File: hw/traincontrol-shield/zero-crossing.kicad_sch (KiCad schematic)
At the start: 3 parts, among them U2 H11AA1

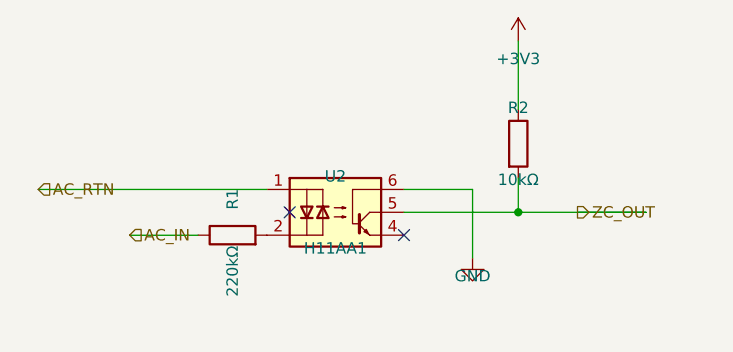
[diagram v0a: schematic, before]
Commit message: Fix U2 (H11AA1) zero-crossing wiring: emitter→GND, base→NC
KiCad symbol coords use y-up convention, so schematic positions
are cy ∓ symbol_y.  Pin 4 (Emitter) is at cy+2.54 (lower-right)
and Pin 6 (Base) is at cy-2.54 (upper-right) — the previous code
had these swapped, connecting GND to the base and NC to the emitter.

Co-Authored-By: Claude Sonnet 4.6 <noreply@anthropic.com>
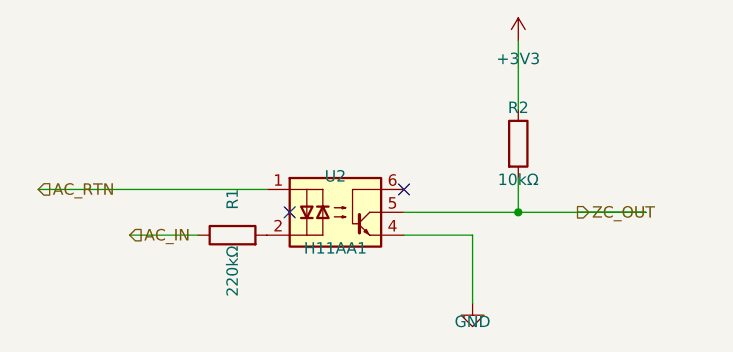
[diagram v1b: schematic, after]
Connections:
- net GND: now also U2.4; no longer U2.6
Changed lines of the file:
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@@
 	)
 	(wire
-		(pts (xy 104.14 87.63) (xy 111.76 87.63))
+		(pts (xy 104.14 92.71000000000001) (xy 111.76 92.71000000000001))
 		(stroke (width 0) (type solid))
 	)
 	(wire
-		(pts (xy 111.76 87.63) (xy 111.76 95.25))
+		(pts (xy 111.76 92.71000000000001) (xy 111.76 100.33000000000001))
 		(stroke (width 0) (type solid))
 	)
 	(symbol
 		(lib_id "power:GND")
-		(at 111.76 95.25 0)
+		(at 111.76 100.33000000000001 0)
 		(unit 1)
 		(exclude_from_sim no)
@@
 		(dnp no)
 		(property "Reference" "#PWR0301"
-			(at 111.76 93.25 0)
+			(at 111.76 98.33000000000001 0)
 			(effects (font (size 1.27 1.27)) (hide yes))
 		)
 		(property "Value" "GND"
-			(at 111.76 97.25 0)
+			(at 111.76 102.33000000000001 0)
 			(effects (font (size 1.27 1.27)))
 		)
 		(property "Footprint" ""
-			(at 111.76 95.25 0)
+			(at 111.76 100.33000000000001 0)
 			(effects (font (size 1.27 1.27)) (hide yes))
 		)
 		(property "Datasheet" ""
-			(at 111.76 95.25 0)
+			(at 111.76 100.33000000000001 0)
 			(effects (font (size 1.27 1.27)) (hide yes))
 		)
@@
 	)
 	(no_connect
-		(at 104.14 92.71000000000001)
+		(at 104.14 87.63)
 	)
 	(sheet_instances

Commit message: Fix hierarchical label orientations: angle=0 → angle=180 throughout
All hlabel calls in zero-crossing, xor-interlock, opto-triac-drive, and
rail-voltage-sense sub-sheets were using angle=0, causing the label arrows
to point in the wrong direction. Changed to angle=180 uniformly; for
left-side labels also shifted x by −STUB so the label connection pin
coincides with the circuit element, keeping the label body outside the
schematic area.

Co-Authored-By: Claude Sonnet 4.6 <noreply@anthropic.com>
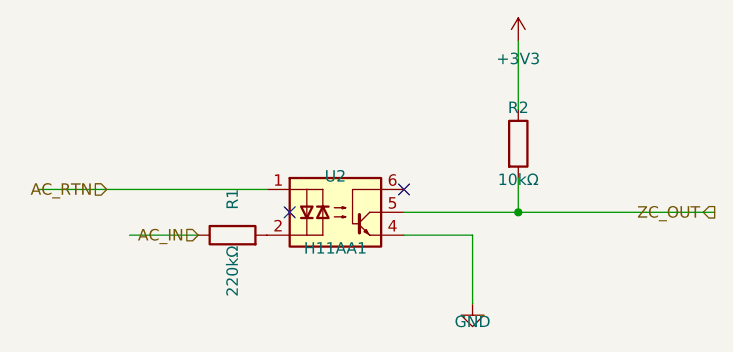
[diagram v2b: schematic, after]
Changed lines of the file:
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@@
 	(hierarchical_label "AC_IN"
 		(shape input)
-		(at 73.66 92.71 0)
+		(at 81.28 92.71 180)
 		(fields_autoplaced yes)
-		(effects (font (size 1.27 1.27)) (justify left bottom))
+		(effects (font (size 1.27 1.27)) (justify right bottom))
 		(property "Intersheetrefs" "${INTERSHEET_REFS}"
-			(at 73.66 92.71 0)
+			(at 81.28 92.71 0)
 			(effects (font (size 1.27 1.27)) (hide yes))
 		)
 	)
 	(wire
-		(pts (xy 63.50000000000001 87.63) (xy 71.12 87.63))
+		(pts (xy 63.5 87.63) (xy 71.12 87.63))
 		(stroke (width 0) (type solid))
 	)
 	(hierarchical_label "AC_RTN"
 		(shape input)
-		(at 63.50000000000001 87.63 0)
+		(at 71.12 87.63 180)
 		(fields_autoplaced yes)
-		(effects (font (size 1.27 1.27)) (justify left bottom))
+		(effects (font (size 1.27 1.27)) (justify right bottom))
 		(property "Intersheetrefs" "${INTERSHEET_REFS}"
-			(at 63.50000000000001 87.63 0)
+			(at 71.12 87.63 0)
 			(effects (font (size 1.27 1.27)) (hide yes))
 		)
 	)
 	(wire
-		(pts (xy 123.41999999999999 90.17) (xy 131.04 90.17))
+		(pts (xy 131.04 90.17) (xy 138.66 90.17))
 		(stroke (width 0) (type solid))
 	)
 	(hierarchical_label "ZC_OUT"
 		(shape output)
-		(at 123.41999999999999 90.17 0)
+		(at 138.66 90.17 180)
 		(fields_autoplaced yes)
-		(effects (font (size 1.27 1.27)) (justify left bottom))
+		(effects (font (size 1.27 1.27)) (justify right bottom))
 		(property "Intersheetrefs" "${INTERSHEET_REFS}"
-			(at 123.41999999999999 90.17 0)
+			(at 138.66 90.17 0)
 			(effects (font (size 1.27 1.27)) (hide yes))
 		)
